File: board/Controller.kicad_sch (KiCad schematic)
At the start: 13 parts, among them Q1 PSMN5R2-60YL, U1 LT4275AIDDPBF-LT4275AIDDPBF

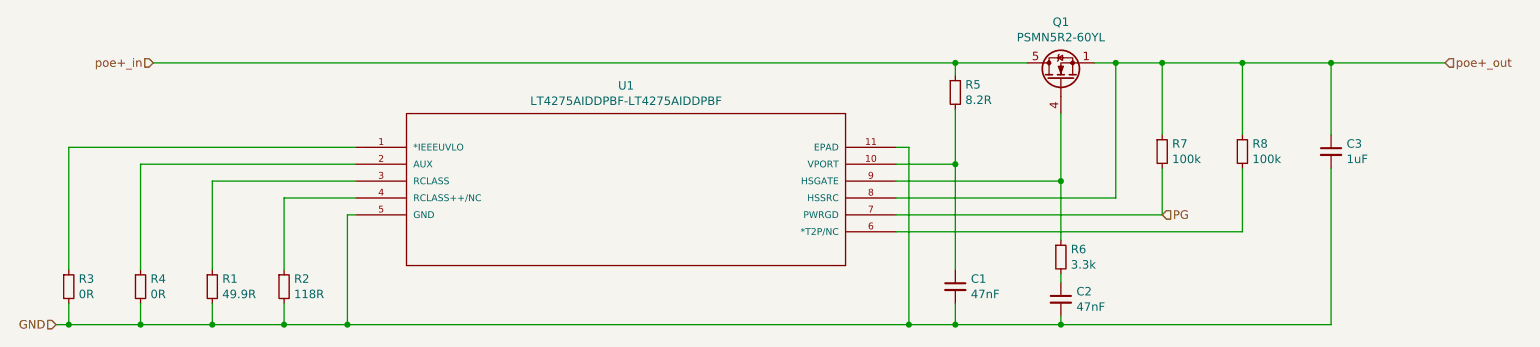
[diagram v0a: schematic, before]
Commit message: updated connectors
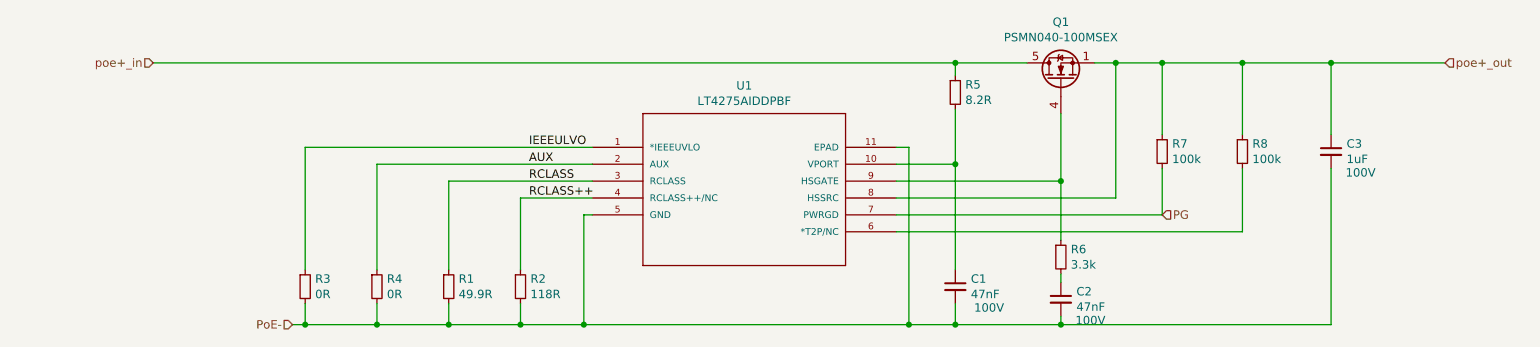
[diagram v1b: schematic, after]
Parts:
- C1, C2: Voltage (none) -> 100V
- C3: Voltage 100 -> 100V
- Q1: value PSMN5R2-60YL -> PSMN040-100MSEX; footprint Package_TO_SOT_SMD:LFPAK56 -> Package_TO_SOT_SMD:LFPAK33
- U1: value LT4275AIDDPBF-LT4275AIDDPBF -> LT4275AIDDPBF; footprint Package_DFN_QFN:DFN-10-1EP_3x3mm_P0.5mm_EP1.65x2.38mm -> Package_DFN_QFN:DFN-10-1EP_3x3mm_P0.5mm_EP1.65x2.38mm_ThermalVias; symbol board-rescue:LT4275AIDDPBF-LT4275AIDDPBF-Auto-Intern-parts -> b027:LT4275AIDDPBF
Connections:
- net IEEEULVO: now reaches R3.1, U1.1 (*IEEEUVLO)
- net AUX: now reaches R4.1, U1.2 (AUX)
- net RCLASS: now reaches R1.1, U1.3 (RCLASS)
- net RCLASS++: now reaches R2.1, U1.4 (RCLASS++/NC)
- net GND renamed PoE-
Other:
- moved on the sheet: R1, R2, R3, R4, U1
